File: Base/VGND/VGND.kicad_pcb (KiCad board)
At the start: 2 copper layers, 30 x 84 mm, 35 parts, among them J1 Conn_01x04_Pin, J2 Conn_01x05_Pin, J3 Barrel_Jack_Switch, J4 AudioJack2_Ground, J5 AudioJack2_Ground, Q1 40V, U1 TLE2426xD, U2 OPA1656

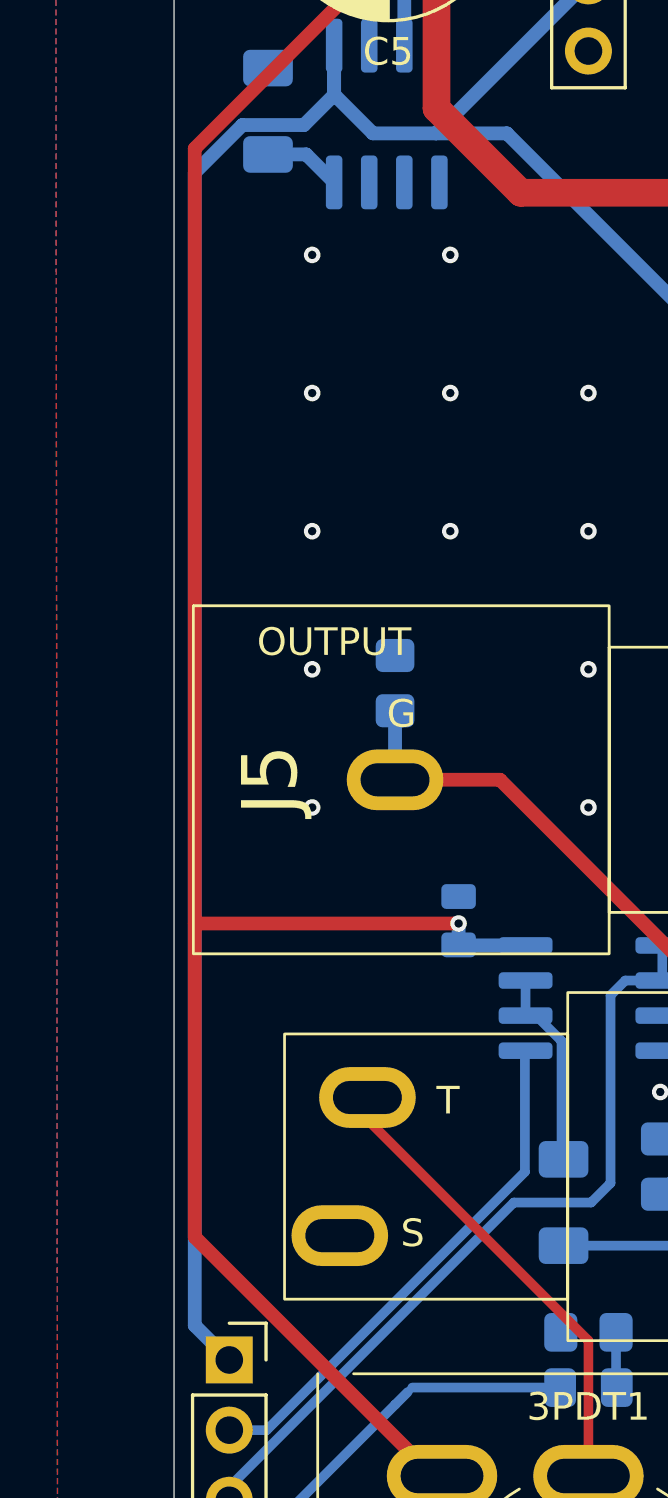
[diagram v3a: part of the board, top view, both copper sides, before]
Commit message: VGND: Add capacitor to GNDREF for stability
The base boards should use GNDREF purely as a voltage reference, but
let's face it, they haven't always done that.  Hopefully no longer
calling it GND will keep it from happening, but this adds a small
capacitor to it in the hope that it will help keep it stable.

The TLE2426 datasheet has a graph of the stability range on pg 17 on
load current vs load capacitance, and that says that it should be stable
with a load capacitance in the 1uF-100uF range for all valid output
currents (+-20mA).

So adding a 10uF capacitor on the base board should be the safe thing to
do.  There's nothing we can do if the effect board just pulls or sinks
more current than the 20mA that the TLE2426 supports, but we can at
least stay off the documented unstable region.

[ From a quick look through the effect boards, it looks like we should
  be good. GNDREF is typically used with the inverting input of an
  op-amp. Or alternatively with sufficiently big resistors to the
  signal, ie tens of kOhms or more. Fingers crossed. ]

Also fix the incorrect commentary about 80mA current capability on the
schematic sheet.  I wonder where I picked that incorrect value from.  I
must have been looking at the wrong part.  Or on some bad meds.

Signed-off-by: Linus Torvalds <torvalds@linux-foundation.org>
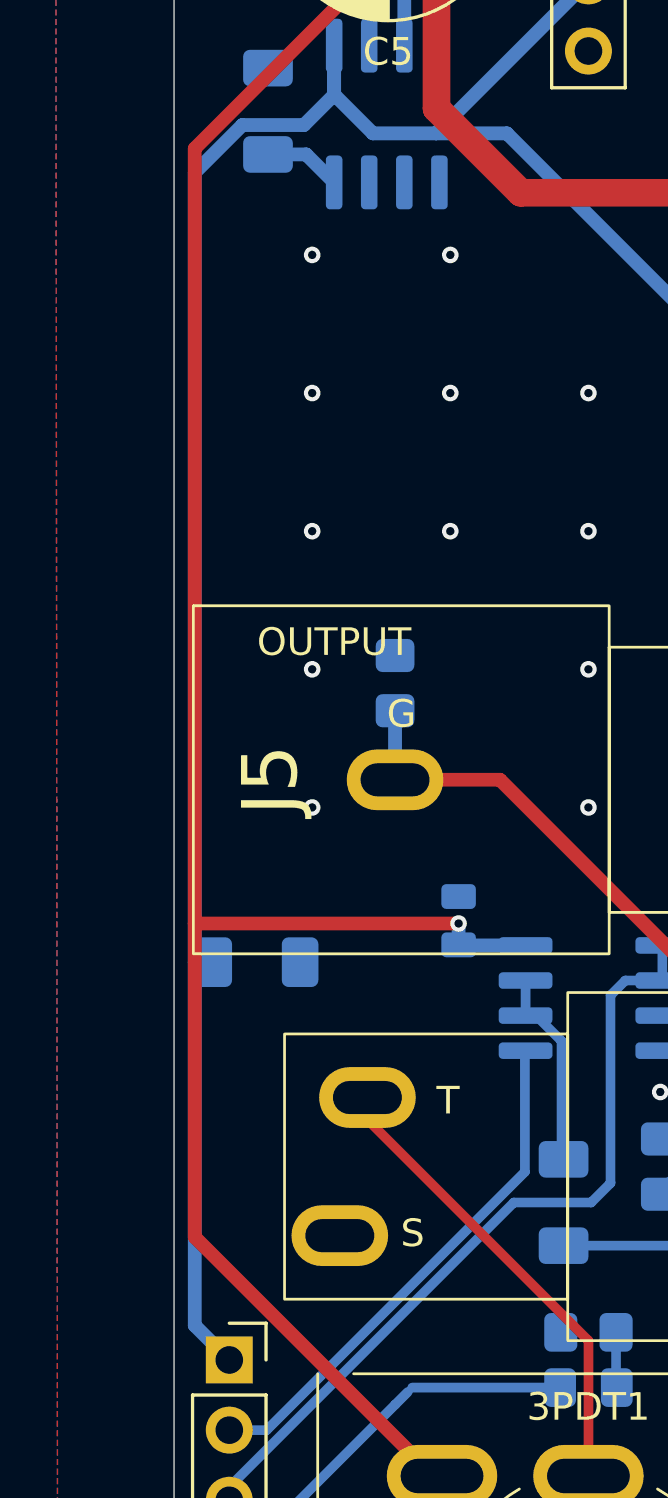
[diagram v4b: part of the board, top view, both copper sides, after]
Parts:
- added C6: 10uF, Capacitor_SMD:C_1206_3216Metric_Pad1.33x1.80mm_HandSolder, B.Cu at (88.0, 110.6)
- renumbered C9 to C10, C6 to C7, C7 to C8, C8 to C9
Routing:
- net GNDREF: track 113.9 -> 114.6 mm

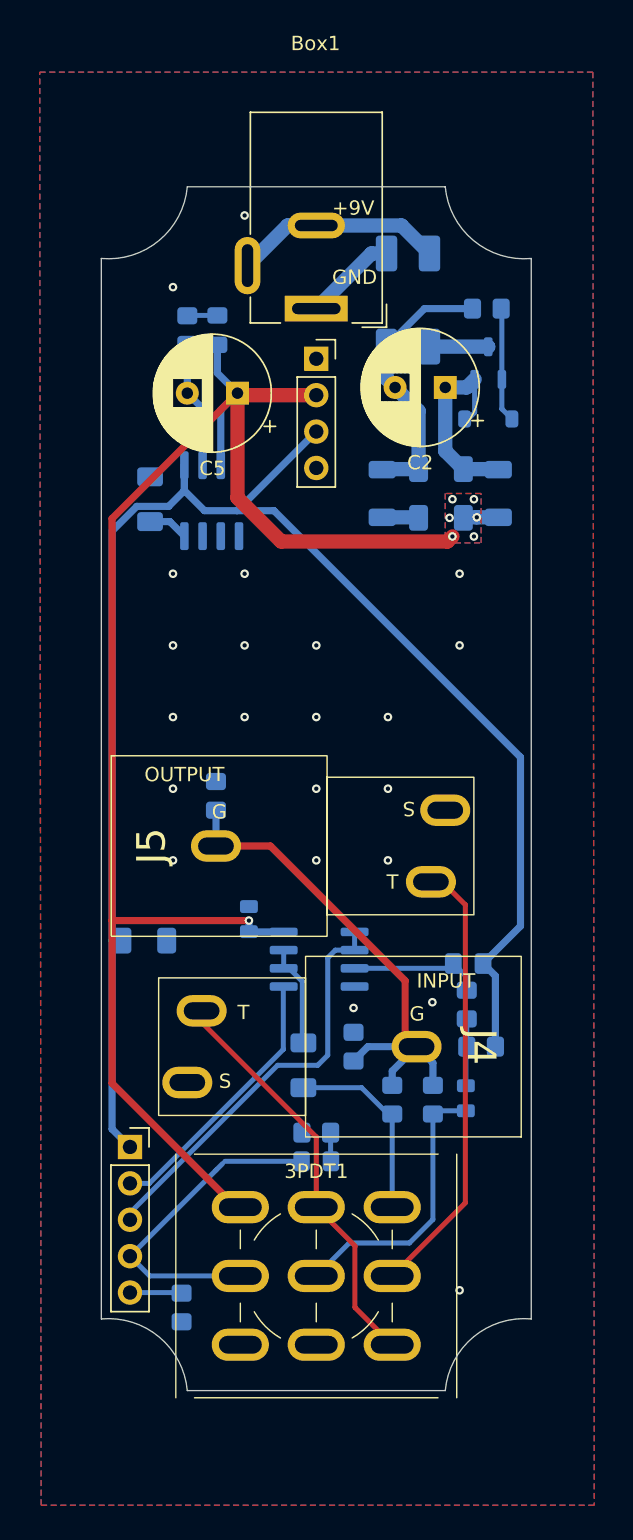
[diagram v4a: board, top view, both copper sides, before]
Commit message: VGND: use the Würth reverse-mounted LEDs
Let's make those pointless status lights that you can't see in an
enclosure really fancy.

Because let's face it, most of my testing is without enclosures.

Signed-off-by: Linus Torvalds <torvalds@linux-foundation.org>
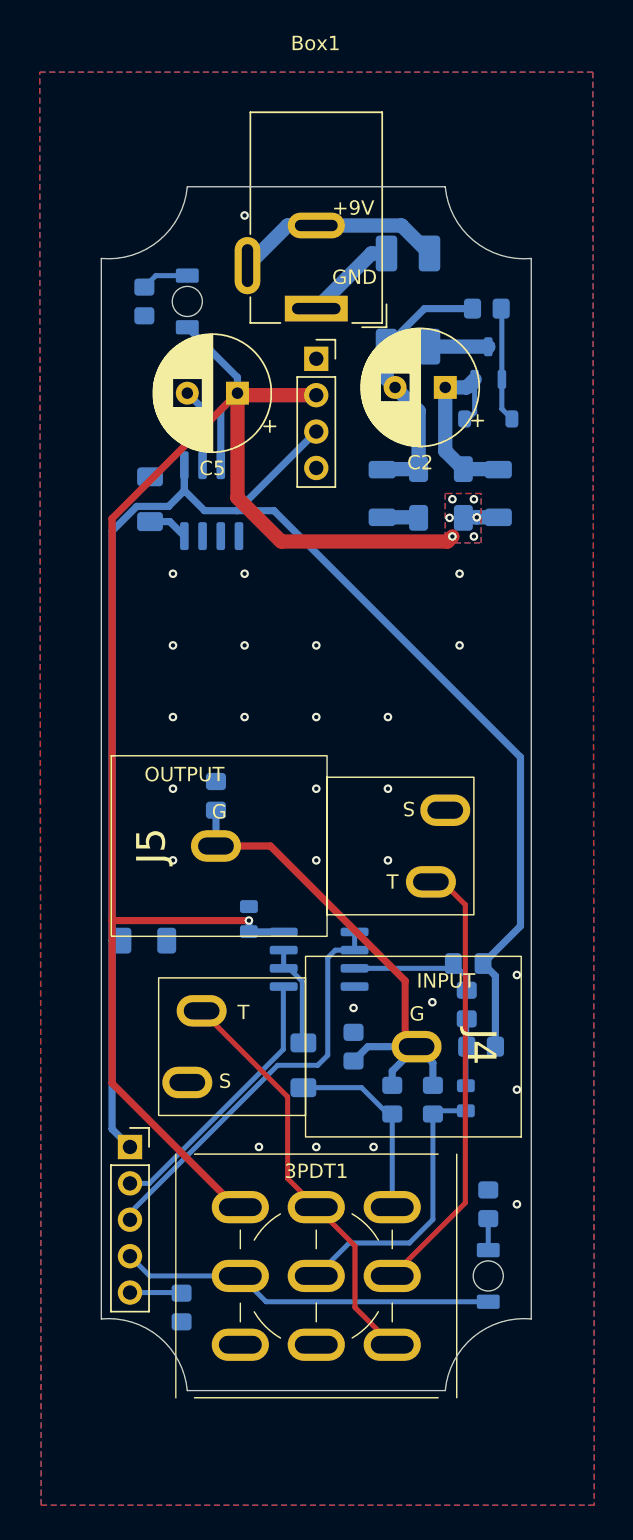
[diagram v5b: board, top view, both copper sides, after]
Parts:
- D2, D3: footprint LED_SMD:LED_0805_2012Metric_Pad1.15x1.40mm_HandSolder -> Mylib:Würth Reverse Mount LED
- moved D3 14.4 mm to (112.0, 134.0), turned to -90 degrees
- moved R10 13.0 mm to (112.0, 129.0), turned to 90 degrees
- moved R9 3.61 mm to (88.0, 66.0)
- moved D2 2.90 mm to (91.0, 66.0)
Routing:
- net GND: track 11.4 -> 8.02 mm, vias 22 -> 26
- net LED+: track 23.0 -> 26.3 mm
- net VIN: track 118.1 -> 120.2 mm
- net Net-(D2-K): track 2.11 -> 3.33 mm

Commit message: Simplify base board GND noise isolation
I finally ended up building multiple test boards to actually check the
experimental parts of the ground isolation.

It turns out none of it helps reduce noise, and the actual ground loop
isolation resistors actively hurt.

It also turns out that the biggest source of noise is actually my
soldering station.  Turning that off when looking at the signals on the
oscilloscope makes quite a noticeable difference ;)

Maybe the ground loop resistors might help in some special situations,
but when looking at a signal generator on the scope they most definitely
hurt.  Having good grounding everywhere is just better.

And I much prefer the "ground everything in a good ground plane" over
the alternatives, particularly since it simplifies things too.  So let's
end that experiment.

Also removing the common mode choke and the ferrite on the ground input
path.  They weren't noticeable in any test, and I think improving the
power supply side is the better option.

Finally - I like the reverse-mounted LEDs, but for the base board they
end up eventaully invisible, and since we need to have the "real" LED
for the stomp switch indicator, they are cute but not really productive.
So they are gone again.

Signed-off-by: Linus Torvalds <torvalds@linux-foundation.org>
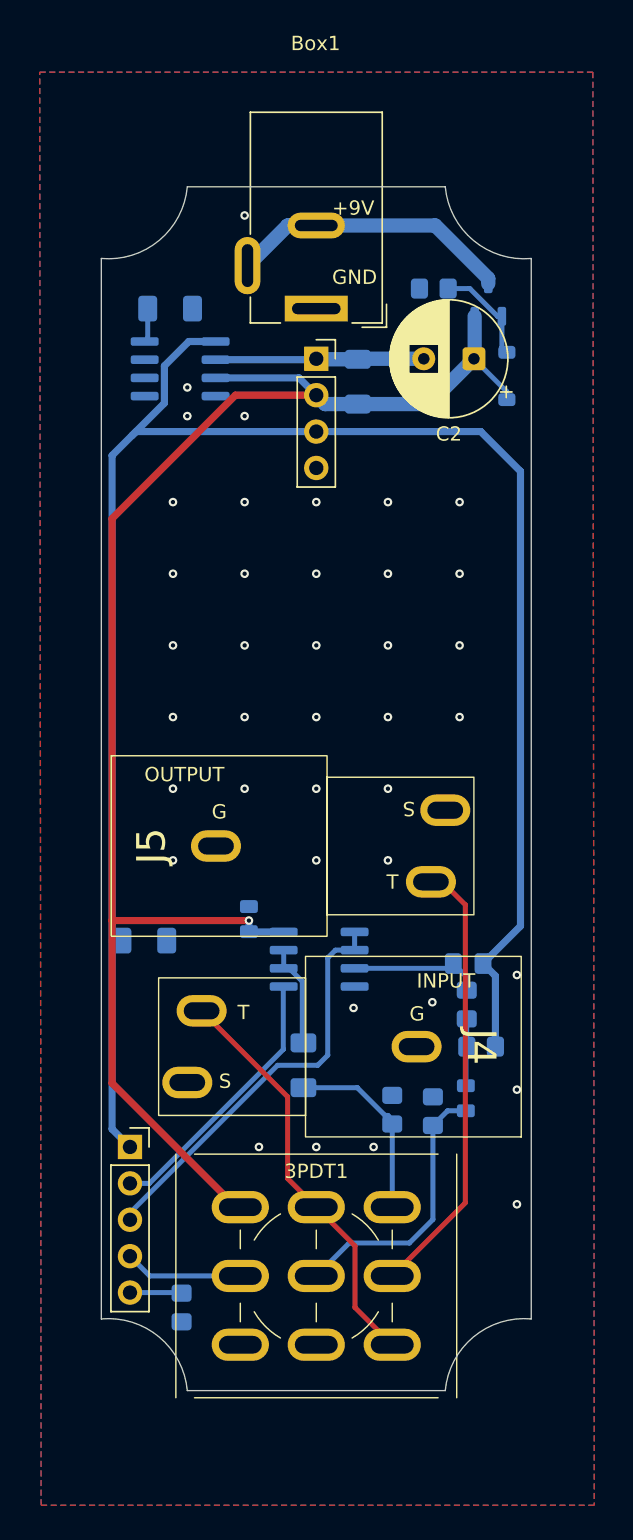
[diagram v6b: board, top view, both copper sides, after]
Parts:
- removed C4: 10uF, Capacitor_SMD:C_1206_3216Metric_Pad1.33x1.80mm_HandSolder
- removed C5: 100uF, Capacitor_THT:CP_Radial_D8.0mm_P3.50mm
- removed D2, D3: LED_Small, Mylib:Würth Reverse Mount LED
- removed FB1, FB2: FerriteBead, Inductor_SMD:L_1206_3216Metric_Pad1.22x1.90mm_HandSolder
- removed FL1: ACM7060, Inductor_SMD:L_CommonModeChoke_TDK_ACM7060
- removed R10, R9: 10k, Resistor_SMD:R_0805_2012Metric_Pad1.20x1.40mm_HandSolder
- removed R6, R7: 10R, Resistor_SMD:R_0805_2012Metric_Pad1.20x1.40mm_HandSolder
- moved C1 13.4 mm to (89.8, 66.5), turned to 0 degrees
- moved U1 9.46 mm to (90.5, 70.7), turned to 180 degrees
- moved C3 8.42 mm to (102.9, 71.6), turned to 90 degrees
- moved Q1 4.40 mm to (112.0, 65.9)
- moved R1 3.96 mm to (108.2, 65.1)
- moved D1 3.27 mm to (113.3, 71.2), turned to 90 degrees
- moved C2 2.83 mm to (111.0, 70.0)
- moved R4 0.80 mm to (108.1, 122.5)
- moved R8 0.70 mm to (105.3, 122.4)
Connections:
- C2 pad 1: Net-(D1-K) -> VIN
- C2 pad 2: GNDIN -> GND
- C3 pad 1: Net-(D1-K) -> VIN
- C3 pad 2: GNDIN -> GND
- D1 pad 1: Net-(D1-K) -> VIN
- J3 pad 1: Net-(FL1-Pad1) -> GND
- J3 pad 2: Net-(FL1-Pad2) -> PWRIN
- J3 pad 3: Net-(FL1-Pad2) -> PWRIN
- J4 pad G: GNDS -> GND
- J5 pad G: GNDS -> GND
- Q1 pad 2: Net-(D1-K) -> VIN
- R1 pad 2: GNDIN -> GND
- R4 pad 2: GNDS -> GND
- R8 pad 2: GNDS -> GND
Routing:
- net GNDS: track 34.8 -> 0.00 mm
- net GNDIN: track 19.1 -> 0.00 mm
- net LED+: track 26.3 -> 8.27 mm
- net GNDREF: track 114.6 -> 131.4 mm
- net PWRIN: track 4.11 -> 19.9 mm
- net Net-(FL1-Pad2): track 14.7 -> 0.00 mm
- net Net-(D1-K): track 14.2 -> 0.00 mm
- net VIN: track 120.2 -> 109.2 mm, vias 7 -> 1
- net GND: track 8.02 -> 14.6 mm, vias 26 -> 39
- net Net-(FL1-Pad1): track 6.49 -> 0.00 mm
- net Net-(D2-K): track 3.33 -> 0.00 mm
- net Net-(D3-K): track 2.20 -> 0.00 mm
- net Net-(D1-A): track 8.01 -> 7.21 mm
- net OUT^{RAW}: track 13.5 -> 12.9 mm
- removed copper zone on B.Cu, net VIN
- removed copper zone on F.Cu, net VIN

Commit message: Update footprint for the 6.35mm mono jack
This was one of the first footprints I did, and I did it oddly, with the
center point of the footprint in a strange random place.

Also, some of the measurements for the courtyard and silkscreen weren't
quite right, which I think was a result of partly doing it with calipers
and partly looking at the datasheet.  The fact that the origin for the
footprint was odd made it not very obvious.

So center the footprint on the central ground pin, which is what most of
the datasheet measurements are referenced off.

And while those issues were mostly cosmetic, there were a couple of real
issues with the footprint too.  The hole for the tip and switch pad was
annoyingly tight: the datasheet says they are 2.5mm wide, and that was
the exact size of the hole.  Yes, it worked, and certainly kept the
component in place, but it was always a slight annoyance.

A bigger annoyance was that because the 1590A build is so tight
vertically, I always ended up snipping off the plastic standoffs / feet
on the jack.  They make the jack be 12mm high, and cutting them off
saves about 0.75mm of vertical space.

But I did it mostly because I didn't want to bother with the footprint
definition, and partly because the alternative to cutting off the feet
was to have mechanical holes in the PCB, and I felt that board space was
too valuable.

Now, it turns out that board space isn't all that valuable on the base
board - there just aren't that many components there - and since I
wanted to fix up the other mostly cosmetic issues, I felt that not
having to use flush cutters on the jacks when assembling it is the
better option.

This all means that the boards that have these footprints need to be
updated for the re-positioning and the mechanical holes that mean that
you can't place components and traces on either side.  But it's really
just the regular base board and the trivial debug board that need some
TLC.

While doing that, I also moved the connectors out eve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
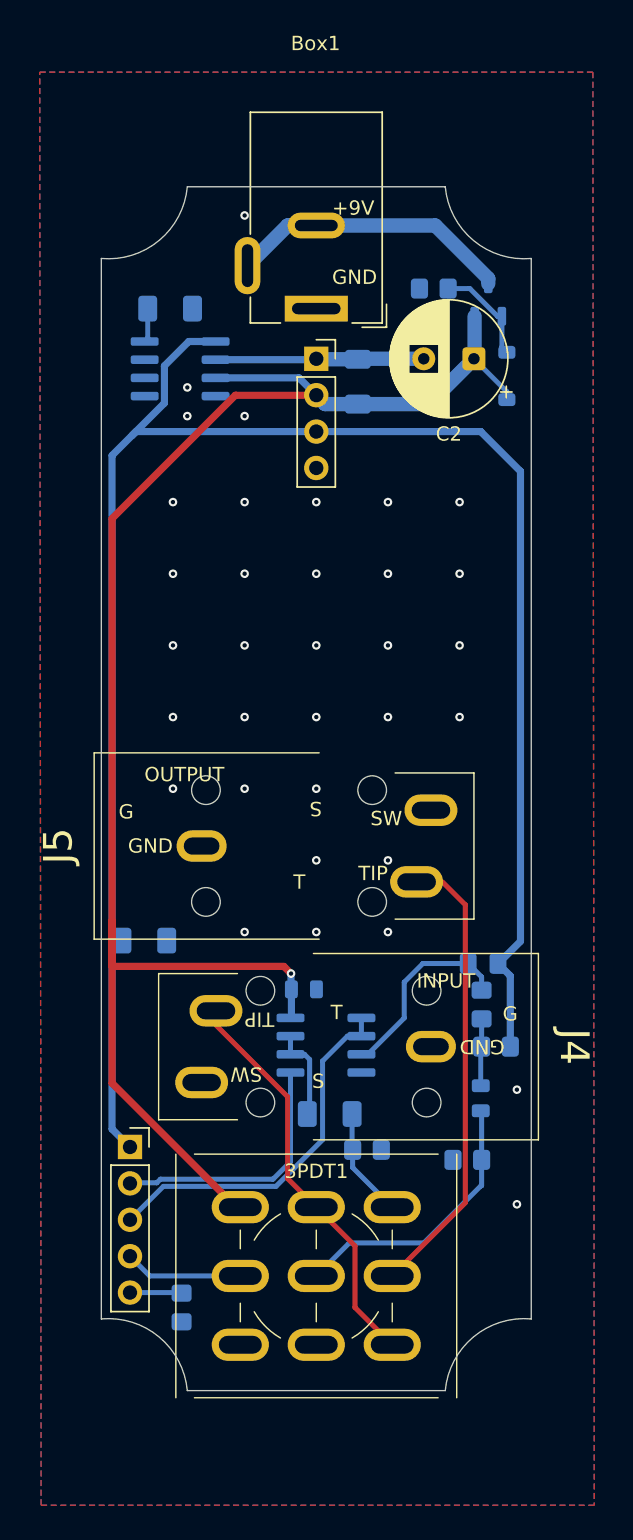
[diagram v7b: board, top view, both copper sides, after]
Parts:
- moved J4 6.50 mm to (108.0, 118.0)
- moved J5 6.50 mm to (92.0, 104.0)
- moved C7 6.22 mm to (99.1, 114.0), turned to 0 degrees
- moved U2 6.02 mm to (100.7, 117.9)
- moved R4 4.16 mm to (110.5, 125.9), turned to 180 degrees
- moved C10 3.86 mm to (100.9, 122.7), turned to 180 degrees
- moved R8 3.31 mm to (103.5, 125.2), turned to 0 degrees
- moved C9 1.04 mm to (111.6, 112.2)
- moved C8 1.04 mm to (111.5, 121.6)
- moved R3 1.04 mm to (111.5, 115.1)
- moved R5 1.04 mm to (112.5, 118.0)
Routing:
- net VIN: track 109.2 -> 115.2 mm
- net OUT^{RAW}: track 12.9 -> 7.16 mm
- net Net-(U2A-+): track 8.80 -> 13.3 mm
- net IN^{EFF}: track 29.2 -> 25.9 mm
- net OUT^{EFF}: track 18.9 -> 18.0 mm
- net GND: track 14.6 -> 14.4 mm, vias 39 -> 34
